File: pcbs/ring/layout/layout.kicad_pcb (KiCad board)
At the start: 2 copper layers, 59.8 x 6.2 mm, 61 parts, among them J1 ?, Q1 CSD13380F3T, Q2 CSD13380F3T, U1 BQ27427YZFR, U2 BQ29700, U3 nRF52833-QDAA, U4 MAX30102EFD+T, U5 LSM6DSOX, U6 TMP117AIDRVR, U7 TPS7A2018PDQN, Y1 32MHz, Y2 32.768kHz

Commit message: more vias
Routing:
- net GND: vias 50 -> 55
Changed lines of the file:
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@@
 	)
 	(via
+		(at 175.6 85.5)
+		(size 0.35)
+		(drill 0.15)
+		(layers "F.Cu" "B.Cu")
+		(free yes)
+		(net 2)
+	)
+	(via
 		(at 145.75 82.8)
 		(size 0.35)
@@
 	)
 	(via
+		(at 171.75 82.2)
+		(size 0.35)
+		(drill 0.15)
+		(layers "F.Cu" "B.Cu")
+		(free yes)
+		(net 2)
+	)
+	(via
+		(at 172.75 81.25)
+		(size 0.35)
+		(drill 0.15)
+		(layers "F.Cu" "B.Cu")
+		(free yes)
+		(net 2)
+	)
+	(via
+		(at 177.25 83.15)
+		(size 0.35)
+		(drill 0.15)
+		(layers "F.Cu" "B.Cu")
+		(free yes)
+		(net 2)
+	)
+	(via
 		(at 157.55 85.7)
 		(size 0.4)
@@
 	)
 	(via
+		(at 177.25 82.2)
+		(size 0.35)
+		(drill 0.15)
+		(layers "F.Cu" "B.Cu")
+		(free yes)
+		(net 2)
+	)
+	(via
 		(at 171.45 83.5)
 		(size 0.35)
@@
 	)
 	(segment
-		(start 176.998853 81.3649)
-		(end 176.816976 81.183023)
+		(start 176.7 83.516047)
+		(end 176.7 81.299999)
 		(width 0.2)
 		(layer "F.Cu")
@@
 	)
 	(segment
-		(start 167.565005 84.050013)
-		(end 171.900013 84.050013)
+		(start 176.7 81.299999)
+		(end 176.816976 81.183023)
 		(width 0.2)
 		(layer "F.Cu")
@@
 	(segment
 		(start 175.066047 85.15)
-		(end 176.998853 83.217194)
+		(end 176.7 83.516047)
 		(width 0.2)
 		(layer "F.Cu")
@@
 	)
 	(segment
-		(start 167.2525 84.3625)
-		(end 167.565005 84.050013)
+		(start 173 85.15)
+		(end 175.066047 85.15)
 		(width 0.2)
 		(layer "F.Cu")
@@
 	)
 	(segment
-		(start 173 85.15)
-		(end 175.066047 85.15)
+		(start 167.2525 84.3625)
+		(end 167.565005 84.050013)
 		(width 0.2)
 		(layer "F.Cu")
@@
 	)
 	(segment
-		(start 176.998853 83.217194)
-		(end 176.998853 81.3649)
+		(start 171.900013 84.050013)
+		(end 173 85.15)
 		(width 0.2)
 		(layer "F.Cu")
@@
 	)
 	(segment
-		(start 171.900013 84.050013)
-		(end 173 85.15)
-		(width 0.2)
-		(layer "F.Cu")
-		(net 27)
-	)
-	(segment
 		(start 139.1375 80.9)
 		(end 139.35 80.6875)
@@
 		(width 0.2)
 		(layer "F.Cu")
+		(net 27)
+	)
+	(segment
+		(start 167.565005 84.050013)
+		(end 171.900013 84.050013)
+		(width 0.2)
+		(layer "F.Cu")

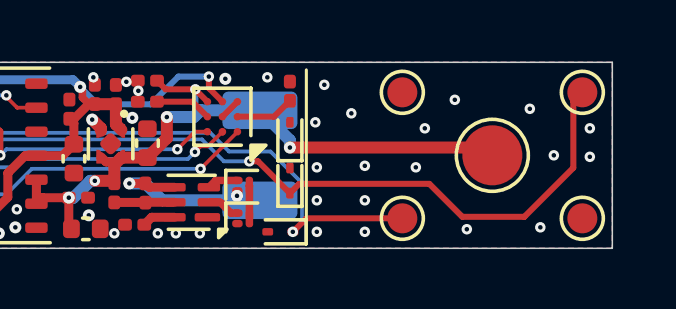
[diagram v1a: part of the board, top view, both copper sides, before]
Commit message: two-sided port
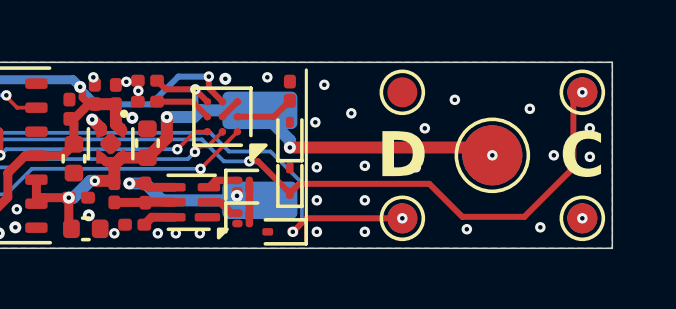
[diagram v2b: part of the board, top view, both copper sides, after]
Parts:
- added TP10: , TestPoint_Pad_D1.0mm:TestPoint_Pad_D1.0mm, B.Cu at (171.0, 85.2)
- added TP2: , TestPoint_Pad_D1.0mm:TestPoint_Pad_D1.0mm, B.Cu at (177.0, 81.0)
- added TP8: , TestPoint_Pad_D2.0mm:TestPoint_Pad_D2.0mm, B.Cu at (174.0, 83.1)
- added TP9: , TestPoint_Pad_D1.0mm:TestPoint_Pad_D1.0mm, B.Cu at (177.0, 85.2)
- renumbered TP2 to TP3, TP3 to TP4, TP4 to TP5, TP5 to TP6, TP6 to TP7
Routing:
- net swdio: vias 2 -> 3
- net swdclk: vias 2 -> 3
- net VBATT: vias 5 -> 6
- net GND: vias 55 -> 56
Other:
- board text added: "C"
- board text added: "D"

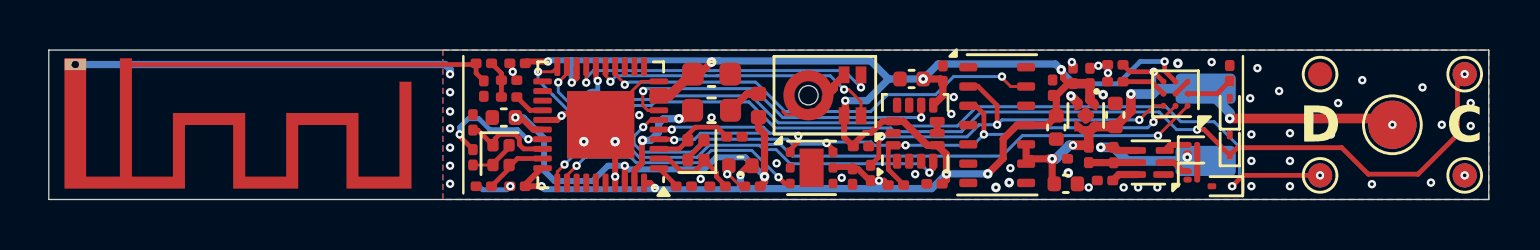
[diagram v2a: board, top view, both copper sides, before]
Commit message: change port spacing
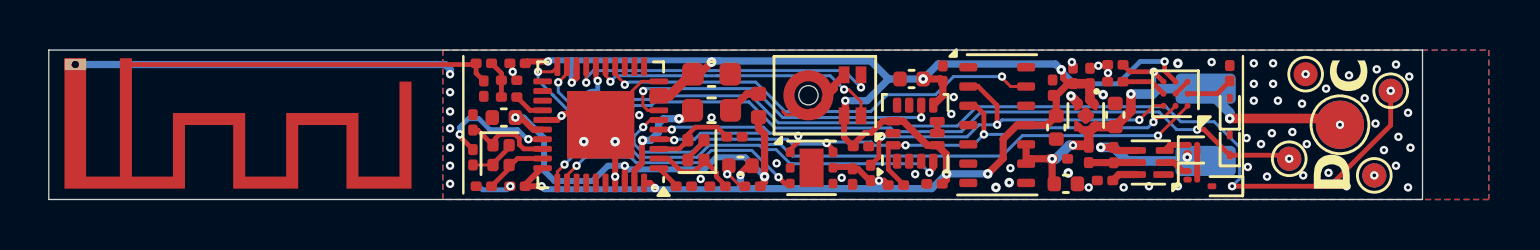
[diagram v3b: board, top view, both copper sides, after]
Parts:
- moved TP2 8.08 mm to (169.7, 84.5)
- moved TP5 8.08 mm to (169.7, 84.5)
- moved TP10 4.57 mm to (173.9, 81.7)
- moved TP4 4.57 mm to (173.9, 81.7)
- moved TP6 3.75 mm to (173.2, 85.2)
- moved TP9 3.75 mm to (173.2, 85.2)
- moved TP3 2.18 mm to (171.8, 83.1)
- moved TP8 2.18 mm to (171.8, 83.1)
- moved TP7 0.60 mm to (170.4, 81.0)
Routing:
- net swdclk: track 45.9 -> 35.3 mm
- net swdio: track 37.4 -> 42.6 mm
- net VBATT: track 23.6 -> 21.4 mm
- net GND: vias 56 -> 69
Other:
- board size 59.8 x 6.2 mm -> 57 x 6.2 mm

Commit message: cleanup
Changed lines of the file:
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@@
 		(net 2)
 		(net_name "GND")
-		(locked yes)
 		(layers "F.Cu" "B.Cu")
 		(hatch edge 0.5)
@@
 		(polygon
 			(pts
-				(xy 134.6 80) (xy 178 80) (xy 178 86.2) (xy 134.6 86.2)
+				(xy 134.6 80) (xy 175.25 80) (xy 175.25 86.2) (xy 134.6 86.2)
 			)
 		)

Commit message: reorganizing
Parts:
- moved TP1 6.41 mm to (147.2, 82.4)
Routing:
- net swdio: track 42.6 -> 1.20 mm, vias 3 -> 1
- net swdclk: track 35.3 -> 1.45 mm, vias 3 -> 1
- net rst: track 1.52 -> 7.31 mm
- net GND: vias 69 -> 65
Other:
- board text removed: "C"
- board text removed: "D"

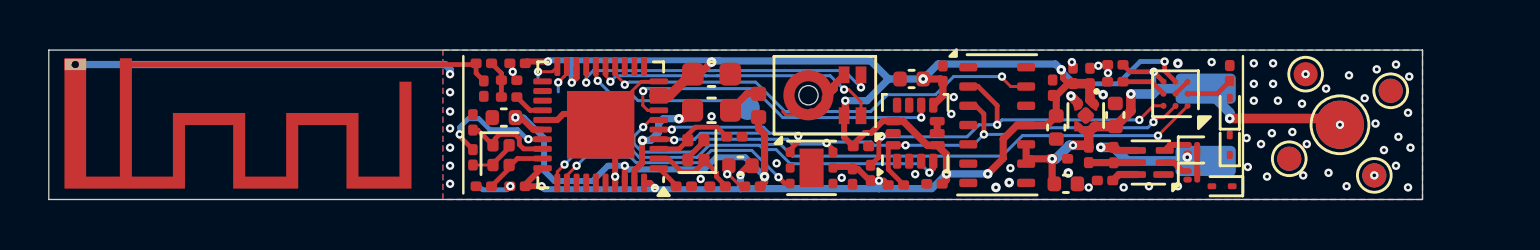
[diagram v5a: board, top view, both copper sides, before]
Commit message: changed connector
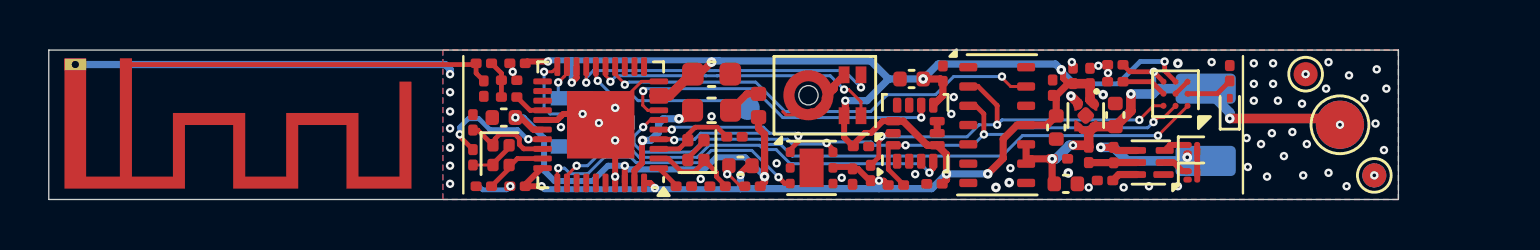
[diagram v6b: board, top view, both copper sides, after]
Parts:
- removed D2, D3: ESD9B5.0ST5G, D_SOD-923:D_SOD-923
- removed TP10: , TestPoint_Pad_D1.0mm:TestPoint_Pad_D1.0mm
- removed the TP2 at (169.7, 84.5)
- removed the TP4 at (173.9, 81.7)
- removed the TP5 at (169.7, 84.5)
- added U6: ?, PinHeader_1x03_P1.00mm_Vertical_SMD_Pin1Left:PinHeader_1x03_P1.00mm_Vertical_SMD_Pin1Left, B.Cu at (140.8, 83.0)
- renumbered TP3 to TP2, TP6 to TP3, TP7 to TP4, TP8 to TP5, TP9 to TP6, U6 to U7, U7 to U8
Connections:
- U3 pad 31: imu_int1 -> tmp_int
- U3 pad 32: tmp_int -> imu_int1
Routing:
- net swdclk: track 1.45 -> 4.65 mm
- net tmp_int: track 10.8 -> 11.5 mm
- net GND: vias 65 -> 66
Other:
- board size 57 x 6.2 mm -> 56 x 6.2 mm

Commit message: reroute
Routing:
- net GND: vias 66 -> 68
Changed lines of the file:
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@@
+	)
+	(via
+		(at 148.35 83.05)
+		(size 0.35)
+		(drill 0.15)
+		(layers "F.Cu" "B.Cu")
+		(free yes)
+		(net 2)
 	)
 	(via
@@
 	(via
 		(at 173.35 80.8)
+		(size 0.35)
+		(drill 0.15)
+		(layers "F.Cu" "B.Cu")
+		(free yes)
+		(net 2)
+	)
+	(via
+		(at 150.3 83.15)
 		(size 0.35)
 		(drill 0.15)
@@
 	)
 	(segment
-		(start 152.45209 83.464899)
-		(end 152.452089 83.4649)
-		(width 0.125)
-		(layer "B.Cu")
-		(net 10)
-	)
-	(segment
 		(start 152.849847 83.5764)
 		(end 152.8 83.5764)
@@
 	)
 	(segment
-		(start 149.5351 83.4649)
+		(start 149.438499 83.561501)
+		(end 149.3495 83.561501)
+		(width 0.125)
+		(layer "B.Cu")
+		(net 10)
+	)
+	(segment
+		(start 149.5 83.5)
 		(end 149.438499 83.561501)
 		(width 0.125)
@@
 	)
 	(segment
+		(start 152.416989 83.5)
+		(end 149.5 83.5)
+		(width 0.125)
+		(layer "B.Cu")
+		(net 10)
+	)
+	(segment
 		(start 144.1 83.3)
 		(end 144.199372 83.200628)
@@
 	)
 	(segment
+		(start 152.8 83.5764)
+		(end 152.6885 83.4649)
+		(width 0.125)
+		(layer "B.Cu")
+		(net 10)
+	)
+	(segment
+		(start 149.236999 83.449)
+		(end 149.3495 83.561501)
+		(width 0.125)
+		(layer "B.Cu")
+		(net 10)
+	)
+	(segment
+		(start 148.149 83.449)
+		(end 149.236999 83.449)
+		(width 0.125)
+		(layer "B.Cu")
+		(net 10)
+	)
+	(segment
+		(start 157.6 83.1)
+		(end 157.8028 82.8972)
+		(width 0.125)
+		(layer "B.Cu")
+		(net 10)
+	)
+	(segment
+		(start 156.35 83.6)
+		(end 152.873447 83.6)
+		(width 0.125)
+		(layer "B.Cu")
+		(net 10)
+	)
+	(segment
+		(start 144.199372 83.200628)
+		(end 147.900628 83.200628)
+		(width 0.125)
+		(layer "B.Cu")
+		(net 10)
+	)
+	(segment
+		(start 152.873447 83.6)
+		(end 152.849847 83.5764)
+		(width 0.125)
+		(layer "B.Cu")
+		(net 10)
+	)
+	(segment
+		(start 147.900628 83.200628)
+		(end 148.149 83.449)
+		(width 0.125)
+		(layer "B.Cu")
+		(net 10)
+	)
+	(segment
+		(start 157.8028 82.8972)
+		(end 163.5 82.8972)
+		(width 0.125)
+		(layer "B.Cu")
+		(net 10)
+	)
+	(segment
+		(start 152.45209 83.464899)
+		(end 152.416989 83.5)
+		(width 0.125)
+		(layer "B.Cu")
+		(net 10)
+	)
+	(segment
 		(start 152.6885 83.4649)
 		(end 152.45209 83.464899)
 		(width 0.125)
 		(layer "B.Cu")
-		(net 10)
-	)
-	(segment
-		(start 149.236999 83.449)
-		(end 149.3495 83.561501)
-		(width 0.125)
-		(layer "B.Cu")
-		(net 10)
-	)
-	(segment
-		(start 148.149 83.449)
-		(end 149.236999 83.449)
-		(width 0.125)
-		(layer "B.Cu")
-		(net 10)
-	)
-	(segment
-		(start 157.6 83.1)
-		(end 157.8028 82.8972)
-		(width 0.125)
-		(layer "B.Cu")
-		(net 10)
-	)
-	(segment
-		(start 156.35 83.6)
-		(end 152.873447 83.6)
-		(width 0.125)
-		(layer "B.Cu")
-		(net 10)
-	)
-	(segment
-		(start 144.199372 83.200628)
-		(end 147.900628 83.200628)
-		(width 0.125)
-		(layer "B.Cu")
-		(net 10)
-	)
-	(segment
-		(start 152.873447 83.6)
-		(end 152.849847 83.5764)
-		(width 0.125)
-		(layer "B.Cu")
-		(net 10)
-	)
-	(segment
-		(start 152.452089 83.4649)
-		(end 149.5351 83.4649)
-		(width 0.125)
-		(layer "B.Cu")
-		(net 10)
-	)
-	(segment
-		(start 152.8 83.5764)
-		(end 152.6885 83.4649)
-		(width 0.125)
-		(layer "B.Cu")
-		(net 10)
-	)
-	(segment
-		(start 147.900628 83.200628)
-		(end 148.149 83.449)
-		(width 0.125)
-		(layer "B.Cu")
-		(net 10)
-	)
-	(segment
-		(start 157.8028 82.8972)
-		(end 163.5 82.8972)
-		(width 0.125)
-		(layer "B.Cu")
-		(net 10)
-	)
-	(segment
-		(start 149.438499 83.561501)
-		(end 149.3495 83.561501)
-		(width 0.125)
-		(layer "B.Cu")

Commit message: added crystal mpns and updated caps
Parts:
- C4, C9: value 12pF -> 5pF
- Y1: value 32MHz -> 8J32076001
- Y2: value 32.768kHz -> 3110M4-32.768DTTLLLL
